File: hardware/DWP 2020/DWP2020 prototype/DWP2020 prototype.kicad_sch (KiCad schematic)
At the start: 2 parts, among them U1 Teensy4.0, U2 SSD1351_128X128_LCD-bGeigieNa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

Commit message: fix some typoos
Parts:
- removed U2: SSD1351_128X128_LCD-bGeigieNanoKit_V1.1r5a-eagle-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, DWP2020 prototype:SSD1351_128X128_LCD, symbol import_from_eagle-rescue:SSD1351_128X128_LCD-bGeigieNanoKit_V1.1r5a-eagle-import
- added U2: SSD1351_128X128, DWP2020 prototype:SSD1351_128X128_LCD, symbol import_from_eagle-rescue:SSD1351_128X128
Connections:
- net at U1.1 (GND): now also U2.JP1$8 (GND)
- net at U1.34 (VUSB): now also U2.JP1$7 (VDD)
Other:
- moved on the sheet: U1
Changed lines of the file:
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@@
-(kicad_sch (version 20200608) (host eeschema "5.99.0-unknown-0bfe413~88~ubuntu18.04.1")
+(kicad_sch (version 20200608) (host eeschema "5.99.0-unknown-08c61e6~88~ubuntu18.04.1")
   (page 1 1)
   (paper "A4")
@@
     (date "2020-06-17")
   )
+  (wire (pts (xy 49.53 27.305) (xy 49.53 38.1))
+    (stroke (width 0) (type solid) (color 0 0 0 0))
+  )
+  (wire (pts (xy 49.53 38.1) (xy 57.15 38.1))
+    (stroke (width 0) (type solid) (color 0 0 0 0))
+  )
+  (wire (pts (xy 113.03 93.98) (xy 118.11 93.98))
+    (stroke (width 0) (type solid) (color 0 0 0 0))
+  )
+  (wire (pts (xy 118.11 40.64) (xy 123.19 40.64))
+    (stroke (width 0) (type solid) (color 0 0 0 0))
+  )
+  (wire (pts (xy 118.11 93.98) (xy 118.11 40.64))
+    (stroke (width 0) (type solid) (color 0 0 0 0))
+  )
+  (wire (pts (xy 119.38 27.305) (xy 49.53 27.305))
+    (stroke (width 0) (type solid) (color 0 0 0 0))
+  )
+  (wire (pts (xy 119.38 38.1) (xy 119.38 27.305))
+    (stroke (width 0) (type solid) (color 0 0 0 0))
+  )
+  (wire (pts (xy 119.38 38.1) (xy 123.19 38.1))
+    (stroke (width 0) (type solid) (color 0 0 0 0))
+  )
   (text "Simple prototype board for software development." (at 274.2692 172.6184 180)
     (effects (font (size 2.5 2.5)) (justify right bottom))
   )
-  (symbol (lib_id "import_from_eagle-rescue:SSD1351_128X128_LCD-bGeigieNanoKit_V1.1r5a-eagle-import") (at 148.59 58.42 0) (unit 1)
+  (symbol (lib_id "import_from_eagle-rescue:SSD1351_128X128") (at 138.43 55.88 0) (unit 1)
     (in_bom yes) (on_board yes)
-    (property "Reference" "U2" (id 0) (at 151.7651 52.0066 0)
+    (property "Reference" "U2" (id 0) (at 130.81 30.48 0)
       (effects (font (size 1.4986 1.4986)) (justify left))
     )
-    (property "Value" "SSD1351_128X128_LCD-bGeigieNanoKit_V1.1r5a-eagle-import" (id 1) (at 151.7651 54.6733 0)
-      (effects (font (size 1.4986 1.4986)) (justify left))
+    (property "Value" "SSD1351_128X128" (id 1) (at 123.19 33.02 0)
+      (effects (font (size 1.499 1.499)) (justify left))
     )
-    (property "Footprint" "DWP2020 prototype:SSD1351_128X128_LCD" (id 2) (at 148.59 58.42 0)
+    (property "Footprint" "DWP2020 prototype:SSD1351_128X128_LCD" (id 2) (at 138.4296 55.8802 0)
       (effects (font (size 1.27 1.27)) hide)
     )
-    (property "Datasheet" "" (id 3) (at 148.59 58.42 0)
+    (property "Datasheet" "" (id 3) (at 138.43 55.88 0)
       (effects (font (size 1.27 1.27)) hide)
     )
   )
-  (symbol (lib_id "Teensy4:Teensy4.0") (at 84.5312 72.8472 0) (unit 1)
+  (symbol (lib_id "Teensy4:Teensy4.0") (at 85.09 72.39 0) (unit 1)
     (in_bom yes) (on_board yes)
-    (property "Reference" "U1" (id 0) (at 84.5312 31.934 0))
-    (property "Value" "Teensy4.0" (id 1) (at 84.5312 34.2327 0))
-    (property "Footprint" "Teensy:Teensy40" (id 2) (at 74.371 67.7674 0)
+    (property "Reference" "U1" (id 0) (at 85.09 31.4768 0))
+    (property "Value" "Teensy4.0" (id 1) (at 85.09 33.7755 0))
+    (property "Footprint" "Teensy:Teensy40" (id 2) (at 74.9298 67.3102 0)
       (effects (font (size 1.27 1.27)) hide)
     )
-    (property "Datasheet" "" (id 3) (at 74.3712 67.7672 0)
+    (property "Datasheet" "" (id 3) (at 74.93 67.31 0)
       (effects (font (size 1.27 1.27)) hide)
     )
@@
       (reference "U1") (unit 1)
     )
-    (path "/620b6ebe-1873-4600-987b-50cce9a7f2c9"
+    (path "/c2fe866b-0538-436e-a065-5c65dd070b82"
       (reference "U2") (unit 1)
     )

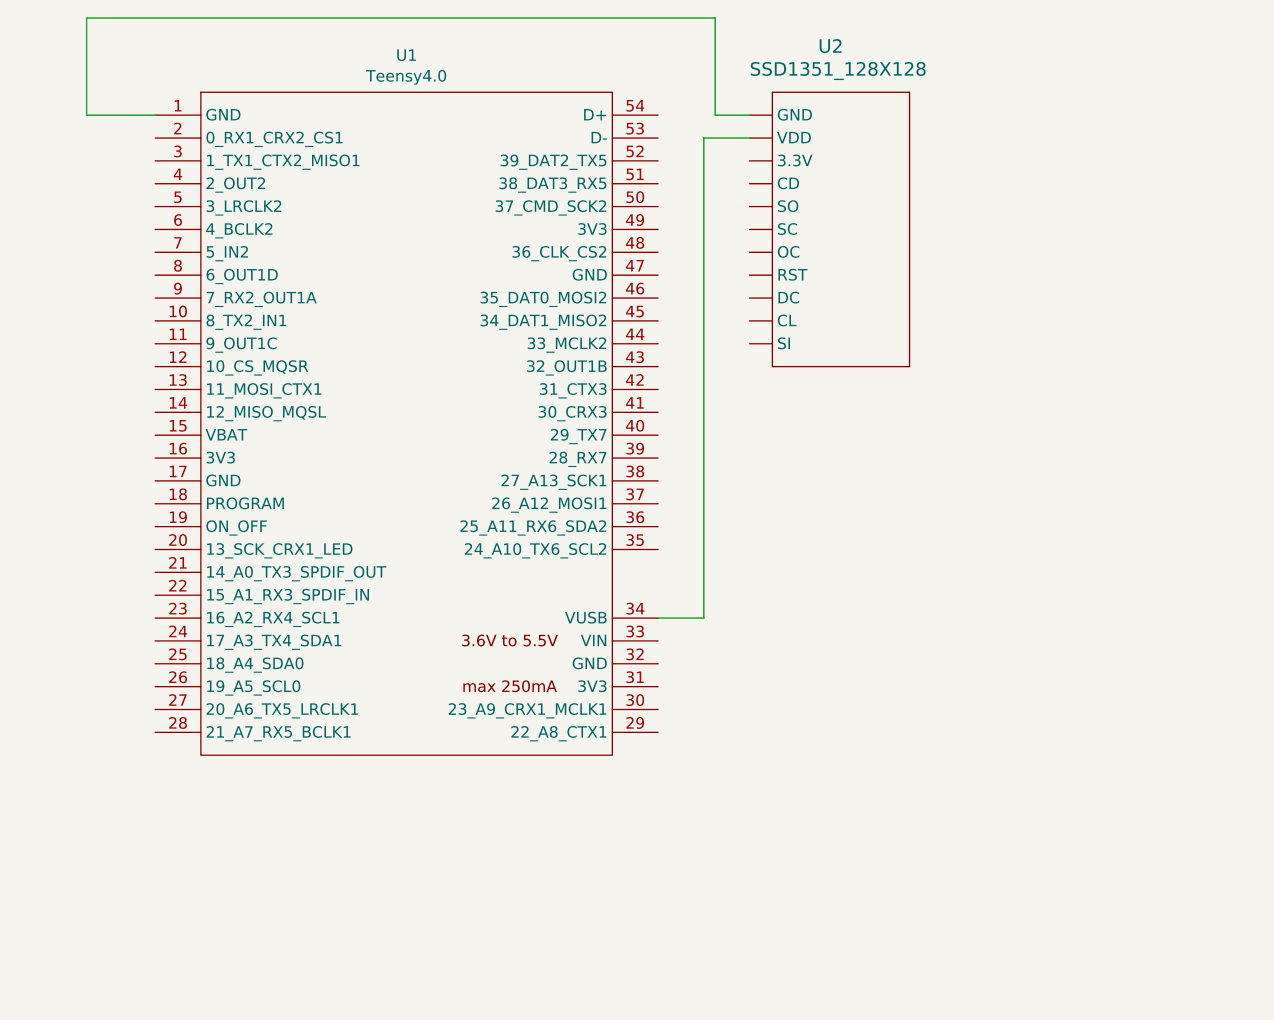
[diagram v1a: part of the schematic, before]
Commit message: Updated ProtoType drawings
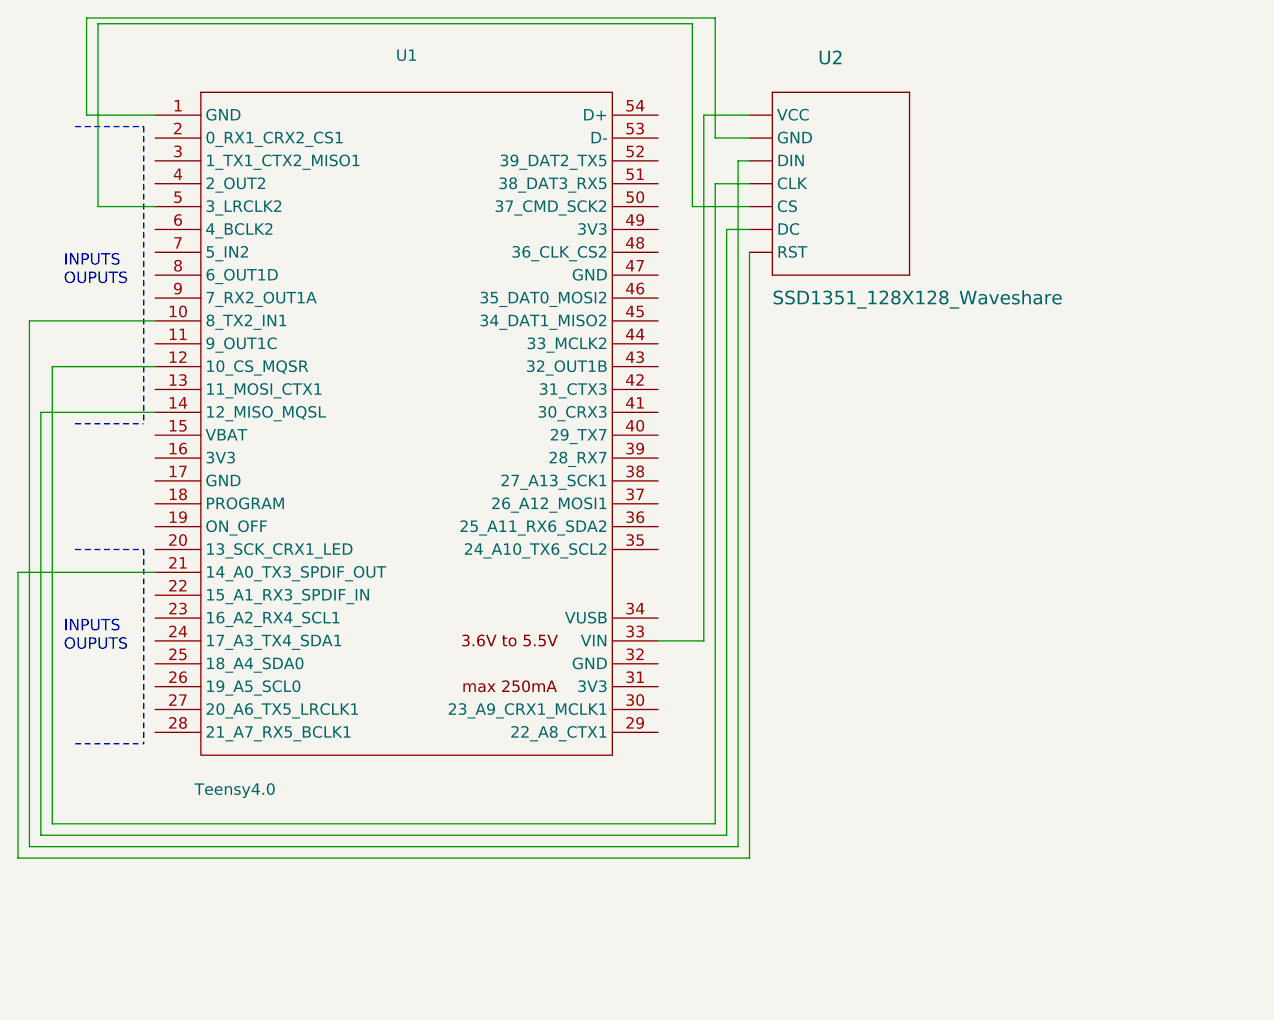
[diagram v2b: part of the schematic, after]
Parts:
- removed U2: SSD1351_128X128, DWP2020 prototype:SSD1351_128X128_LCD, symbol import_from_eagle-rescue:SSD1351_128X128
- added U2: SSD1351_128X128_Waveshare, DWP2020 prototype:SSD1351_128X128_LCD Waveshare, symbol import_from_eagle-rescue:SSD1351_128X128_Waveshare
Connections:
- net at U1.1 (GND): now also U2.JP1$2 (GND)
- net at U1.10 (8_TX2_IN1): now also U2.JP1$3 (DIN)
- net at U1.12 (10_CS_MQSR): now also U2.JP1$4 (CLK)
- net at U1.14 (12_MISO_MQSL): now also U2.JP1$6 (DC)
- net at U1.21 (14_A0_TX3_SPDIF_OUT): now also U2.JP1$7 (RST)
- net at U1.33 (VIN): now also U2.JP1$1 (VCC)
- net at U1.5 (3_LRCLK2): now also U2.JP1$5 (CS)
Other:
- note added: "INPUTS OUPUTS"
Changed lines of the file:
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@@
-(kicad_sch (version 20200608) (host eeschema "5.99.0-unknown-08c61e6~88~ubuntu18.04.1")
+(kicad_sch (version 20200608) (host eeschema "5.99.0-unknown-aa7ce74~88~ubuntu18.04.1")
   (page 1 1)
   (paper "A4")
@@
     (title "Simple Prototype board")
     (date "2020-06-17")
+  )
+  (wire (pts (xy 41.91 88.9) (xy 57.15 88.9))
+    (stroke (width 0) (type solid) (color 0 0 0 0))
+  )
+  (wire (pts (xy 41.91 120.65) (xy 41.91 88.9))
+    (stroke (width 0) (type solid) (color 0 0 0 0))
+  )
+  (wire (pts (xy 43.18 60.96) (xy 43.18 119.38))
+    (stroke (width 0) (type solid) (color 0 0 0 0))
+  )
+  (wire (pts (xy 43.18 119.38) (xy 121.92 119.38))
+    (stroke (width 0) (type solid) (color 0 0 0 0))
+  )
+  (wire (pts (xy 44.45 71.12) (xy 57.15 71.12))
+    (stroke (width 0) (type solid) (color 0 0 0 0))
+  )
+  (wire (pts (xy 44.45 118.11) (xy 44.45 71.12))
+    (stroke (width 0) (type solid) (color 0 0 0 0))
+  )
+  (wire (pts (xy 44.45 118.11) (xy 120.65 118.11))
+    (stroke (width 0) (type solid) (color 0 0 0 0))
+  )
+  (wire (pts (xy 45.72 66.04) (xy 57.15 66.04))
+    (stroke (width 0) (type solid) (color 0 0 0 0))
+  )
+  (wire (pts (xy 45.72 116.84) (xy 45.72 66.04))
+    (stroke (width 0) (type solid) (color 0 0 0 0))
+  )
+  (wire (pts (xy 45.72 116.84) (xy 119.38 116.84))
+    (stroke (width 0) (type solid) (color 0 0 0 0))
   )
   (wire (pts (xy 49.53 27.305) (xy 49.53 38.1))
@@
     (stroke (width 0) (type solid) (color 0 0 0 0))
   )
-  (wire (pts (xy 113.03 93.98) (xy 118.11 93.98))
+  (wire (pts (xy 50.8 27.94) (xy 50.8 48.26))
     (stroke (width 0) (type solid) (color 0 0 0 0))
   )
-  (wire (pts (xy 118.11 40.64) (xy 123.19 40.64))
+  (wire (pts (xy 50.8 48.26) (xy 57.15 48.26))
     (stroke (width 0) (type solid) (color 0 0 0 0))
   )
-  (wire (pts (xy 118.11 93.98) (xy 118.11 40.64))
+  (wire (pts (xy 57.15 60.96) (xy 43.18 60.96))
+    (stroke (width 0) (type solid) (color 0 0 0 0))
+  )
+  (wire (pts (xy 113.03 96.52) (xy 118.11 96.52))
+    (stroke (width 0) (type solid) (color 0 0 0 0))
+  )
+  (wire (pts (xy 116.84 27.94) (xy 50.8 27.94))
+    (stroke (width 0) (type solid) (color 0 0 0 0))
+  )
+  (wire (pts (xy 116.84 48.26) (xy 116.84 27.94))
+    (stroke (width 0) (type solid) (color 0 0 0 0))
+  )
+  (wire (pts (xy 118.11 38.1) (xy 123.19 38.1))
+    (stroke (width 0) (type solid) (color 0 0 0 0))
+  )
+  (wire (pts (xy 118.11 96.52) (xy 118.11 38.1))
     (stroke (width 0) (type solid) (color 0 0 0 0))
   )
@@
     (stroke (width 0) (type solid) (color 0 0 0 0))
   )
-  (wire (pts (xy 119.38 38.1) (xy 119.38 27.305))
+  (wire (pts (xy 119.38 40.64) (xy 119.38 27.305))
     (stroke (width 0) (type solid) (color 0 0 0 0))
   )
-  (wire (pts (xy 119.38 38.1) (xy 123.19 38.1))
+  (wire (pts (xy 119.38 40.64) (xy 123.19 40.64))
     (stroke (width 0) (type solid) (color 0 0 0 0))
+  )
+  (wire (pts (xy 119.38 45.72) (xy 119.38 116.84))
+    (stroke (width 0) (type solid) (color 0 0 0 0))
+  )
+  (wire (pts (xy 120.65 50.8) (xy 120.65 118.11))
+    (stroke (width 0) (type solid) (color 0 0 0 0))
+  )
+  (wire (pts (xy 121.92 43.18) (xy 121.92 119.38))
+    (stroke (width 0) (type solid) (color 0 0 0 0))
+  )
+  (wire (pts (xy 121.92 43.18) (xy 123.19 43.18))
+    (stroke (width 0) (type solid) (color 0 0 0 0))
+  )
+  (wire (pts (xy 123.19 45.72) (xy 119.38 45.72))
+    (stroke (width 0) (type solid) (color 0 0 0 0))
+  )
+  (wire (pts (xy 123.19 48.26) (xy 116.84 48.26))
+    (stroke (width 0) (type solid) (color 0 0 0 0))
+  )
+  (wire (pts (xy 123.19 50.8) (xy 120.65 50.8))
+    (stroke (width 0) (type solid) (color 0 0 0 0))
+  )
+  (wire (pts (xy 123.19 53.34) (xy 123.19 120.65))
+    (stroke (width 0) (type solid) (color 0 0 0 0))
+  )
+  (wire (pts (xy 123.19 120.65) (xy 41.91 120.65))
+    (stroke (width 0) (type solid) (color 0 0 0 0))
+  )
+  (polyline (pts (xy 48.26 39.37) (xy 55.88 39.37))
+    (stroke (width 0) (type dash) (color 0 0 0 0))
+  )
+  (polyline (pts (xy 48.26 72.39) (xy 55.88 72.39))
+    (stroke (width 0) (type dash) (color 0 0 0 0))
+  )
+  (polyline (pts (xy 48.26 86.36) (xy 55.88 86.36))
+    (stroke (width 0) (type dash) (color 0 0 0 0))
+  )
+  (polyline (pts (xy 48.26 107.95) (xy 55.88 107.95))
+    (stroke (width 0) (type dash) (color 0 0 0 0))
+  )
+  (polyline (pts (xy 55.88 39.37) (xy 55.88 72.39))
+    (stroke (width 0) (type dash) (color 0 0 0 0))
+  )
+  (polyline (pts (xy 55.88 86.36) (xy 55.88 107.95))
+    (stroke (width 0) (type dash) (color 0 0 0 0))
+  )
+  (text "INPUTS\nOUPUTS" (at 46.99 57.15 0)
+    (effects (font (size 1.27 1.27)) (justify left bottom))
+  )
+  (text "INPUTS\nOUPUTS" (at 46.99 97.79 0)
+    (effects (font (size 1.27 1.27)) (justify left bottom))
   )
   (text "Simple prototype board for software development." (at 274.2692 172.6184 180)
     (effects (font (size 2.5 2.5)) (justify right bottom))
   )
-  (symbol (lib_id "import_from_eagle-rescue:SSD1351_128X128") (at 138.43 55.88 0) (unit 1)
+  (symbol (lib_id "import_from_eagle-rescue:SSD1351_128X128_Waveshare") (at 138.43 55.88 0) (unit 1)
     (in_bom yes) (on_board yes)
-    (property "Reference" "U2" (id 0) (at 130.81 30.48 0)
-      (effects (font (size 1.4986 1.4986)) (justify left))
-    )
-    (property "Value" "SSD1351_128X128" (id 1) (at 123.19 33.02 0)
+    (property "Reference" "U2" (id 0) (at 130.81 31.75 0)
       (effects (font (size 1.499 1.499)) (justify left))
     )
-    (property "Footprint" "DWP2020 prototype:SSD1351_128X128_LCD" (id 2) (at 138.4296 55.8802 0)
+    (property "Value" "SSD1351_128X128_Waveshare" (id 1) (at 125.73 58.42 0)
+      (effects (font (size 1.499 1.499)) (justify left))
+    )
+    (property "Footprint" "DWP2020 prototype:SSD1351_128X128_LCD Waveshare" (id 2) (at 138.43 55.88 0)
       (effects (font (size 1.27 1.27)) hide)
     )
@@
     (in_bom yes) (on_board yes)
     (property "Reference" "U1" (id 0) (at 85.09 31.4768 0))
-    (property "Value" "Teensy4.0" (id 1) (at 85.09 33.7755 0))
+    (property "Value" "Teensy4.0" (id 1) (at 66.04 113.03 0))
     (property "Footprint" "Teensy:Teensy40" (id 2) (at 74.9298 67.3102 0)
       (effects (font (size 1.27 1.27)) hide)
@@
       (reference "U1") (unit 1)
     )
-    (path "/c2fe866b-0538-436e-a065-5c65dd070b82"
+    (path "/74572b16-3584-4479-b044-a465da731b08"
       (reference "U2") (unit 1)
     )

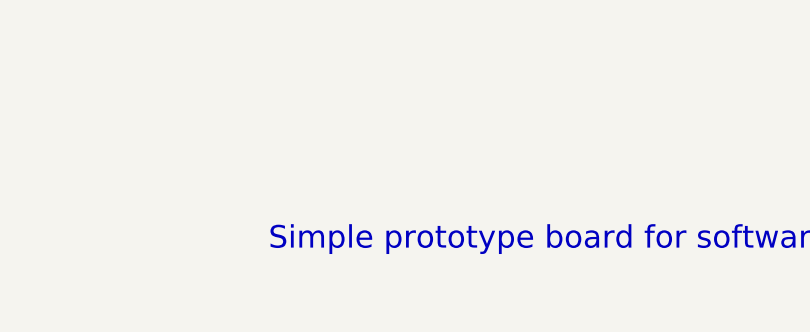
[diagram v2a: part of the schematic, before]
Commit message: Updated schemtics and board
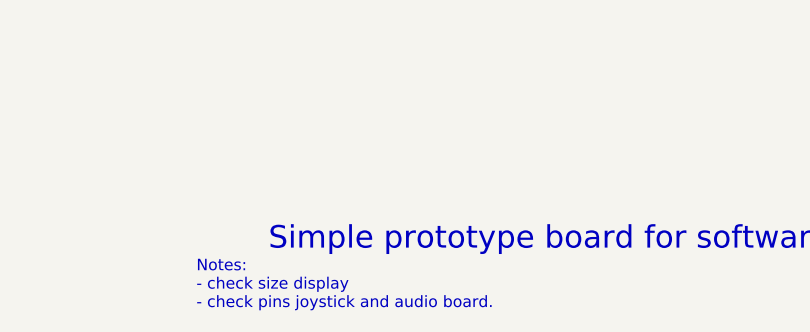
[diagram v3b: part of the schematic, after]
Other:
- note added: "Notes: - check size display - check pins joystick and audio board."
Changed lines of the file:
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@@
-(kicad_sch (version 20200608) (host eeschema "5.99.0-unknown-aa7ce74~88~ubuntu18.04.1")
-  (page 1 1)
+(kicad_sch (version 20200608) (host eeschema "5.99.0-unknown-09cb75b~88~ubuntu18.04.1")
+  (page 2 1)
   (paper "A4")
   (title_block
@@
     (effects (font (size 1.27 1.27)) (justify left bottom))
   )
+  (text "Notes:\n- check size display\n- check pins joystick and audio board."
+    (at 179.07 179.07 0)
+    (effects (font (size 1.27 1.27)) (justify left bottom))
+  )
   (text "Simple prototype board for software development." (at 274.2692 172.6184 180)
     (effects (font (size 2.5 2.5)) (justify right bottom))
   )
-  (symbol (lib_id "import_from_eagle-rescue:SSD1351_128X128_Waveshare") (at 138.43 55.88 0) (unit 1)
+  (symbol (lib_id "import_from_eagle-rescue:SSD1351_128X128_Waveshare") (at 138.43 55.88 0)
     (in_bom yes) (on_board yes)
     (property "Reference" "U2" (id 0) (at 130.81 31.75 0)
@@
     )
   )
-  (symbol (lib_id "Teensy4:Teensy4.0") (at 85.09 72.39 0) (unit 1)
+  (symbol (lib_id "Teensy4:Teensy4.0") (at 85.09 72.39 0)
     (in_bom yes) (on_board yes)
     (property "Reference" "U1" (id 0) (at 85.09 31.4768 0))
